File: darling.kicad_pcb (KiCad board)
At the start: 2 copper layers, 24 x 14 mm, 16 parts, among them J1 USB_C_Receptacle_USB2.0, J2 Conn_01x05, U1 FT230XQ

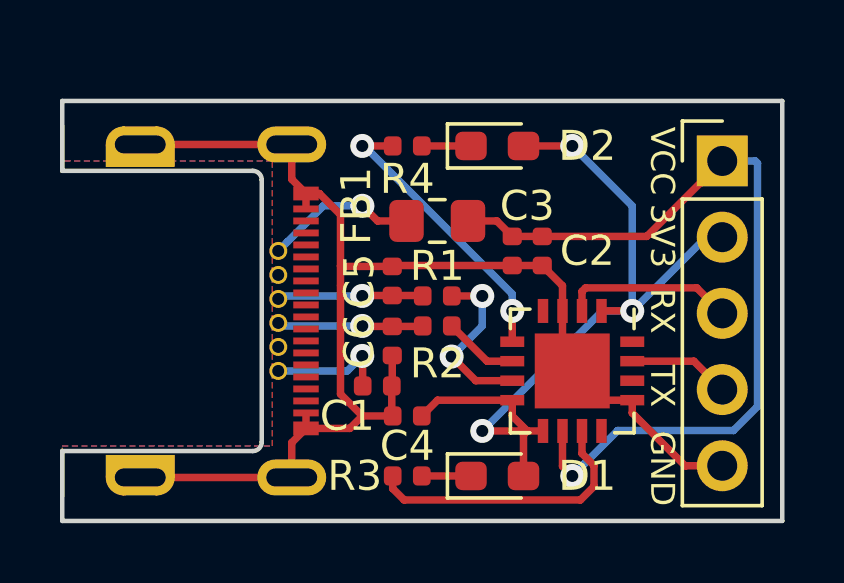
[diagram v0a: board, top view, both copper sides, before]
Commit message: reroute some parts
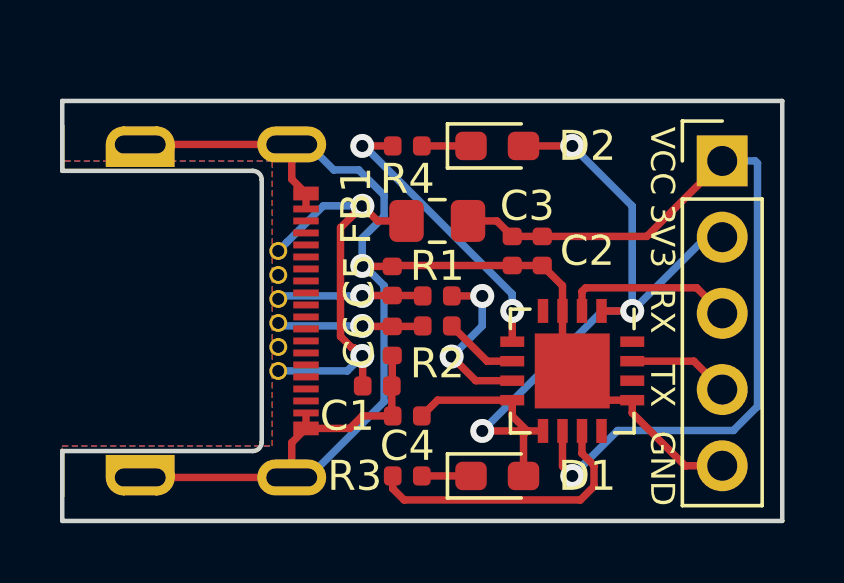
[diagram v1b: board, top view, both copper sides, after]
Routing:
- net GND: track 45.5 -> 51.5 mm, vias 0 -> 1
- net Net-(C1-Pad1): track 9.12 -> 14.8 mm
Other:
- rule trace_min: 0.2 -> 0.125
- rule via_min_size: 0.4 -> 0.6
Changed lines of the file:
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@@
-(kicad_pcb (version 20171130) (host pcbnew 5.1.0)
+(kicad_pcb (version 20171130) (host pcbnew 5.1.1)
   (general
     (thickness 1.6)
     (drawings 23)
-    (tracks 128)
+    (tracks 140)
     (zones 0)
     (modules 16)
@@
     (zone_clearance 0.508)
     (zone_45_only no)
-    (trace_min 0.2)
+    (trace_min 0.125)
     (via_size 0.8)
     (via_drill 0.4)
-    (via_min_size 0.4)
+    (via_min_size 0.6)
     (via_min_drill 0.3)
     (uvia_size 0.3)
@@
   (segment (start 128 125.985) (end 127.985 126) (width 0.25) (layer F.Cu) (net 1))
   (segment (start 128 124.985) (end 128 125.985) (width 0.25) (layer F.Cu) (net 1))
-  (segment (start 126.274999 126.271767) (end 127.003232 127) (width 0.25) (layer F.Cu) (net 1))
-  (segment (start 128 122.015) (end 126.911998 122.015) (width 0.25) (layer F.Cu) (net 1))
-  (segment (start 126.274999 122.651999) (end 126.274999 126.271767) (width 0.25) (layer F.Cu) (net 1))
-  (segment (start 125.57 119.585) (end 126.274999 120.289999) (width 0.25) (layer F.Cu) (net 1))
-  (segment (start 125.125 119.585) (end 125.57 119.585) (width 0.25) (layer F.Cu) (net 1))
-  (segment (start 126.911998 122.015) (end 126.289999 122.015) (width 0.25) (layer F.Cu) (net 1))
-  (segment (start 126.289999 122.015) (end 126.274999 122) (width 0.25) (layer F.Cu) (net 1))
-  (segment (start 126.274999 120.289999) (end 126.274999 122) (width 0.25) (layer F.Cu) (net 1))
-  (segment (start 126.274999 122) (end 126.274999 122.651999) (width 0.25) (layer F.Cu) (net 1))
   (segment (start 125.125 127.415) (end 126.588232 127.415) (width 0.25) (layer F.Cu) (net 1))
   (segment (start 128.03 121.985) (end 128 122.015) (width 0.25) (layer F.Cu) (net 1))
@@
   (segment (start 136 126.9) (end 137.76 128.66) (width 0.25) (layer F.Cu) (net 1))
   (segment (start 136 126.475) (end 136 126.9) (width 0.25) (layer F.Cu) (net 1))
-  (via (at 127.005153 119.994847) (size 0.8) (drill 0.4) (layers F.Cu B.Cu) (net 22))
-  (segment (start 128.475 120.5) (end 127.510306 120.5) (width 0.25) (layer F.Cu) (net 22))
-  (segment (start 127.510306 120.5) (end 127.005153 119.994847) (width 0.25) (layer F.Cu) (net 22))
-  (via (at 127 125) (size 0.8) (drill 0.4) (layers F.Cu B.Cu) (net 22))
-  (segment (start 127.015 126) (end 127.015 125.015) (width 0.25) (layer F.Cu) (net 22))
-  (segment (start 127.015 125.015) (end 127 125) (width 0.25) (layer F.Cu) (net 22))
-  (segment (start 127 125) (end 126.5 125.5) (width 0.25) (layer B.Cu) (net 22))
-  (segment (start 125.705153 119.994847) (end 124.5 121.2) (width 0.25) (layer B.Cu) (net 22))
-  (segment (start 127.005153 119.994847) (end 125.705153 119.994847) (width 0.25) (layer B.Cu) (net 22))
-  (segment (start 124.5 121.2) (end 124.2 121.5) (width 0.25) (layer B.Cu) (net 22))
-  (segment (start 126.5 125.5) (end 124.2 125.5) (width 0.25) (layer B.Cu) (net 22))
+  (segment (start 125.32 119.585) (end 125.125 119.585) (width 0.25) (layer F.Cu) (net 1))
+  (segment (start 125.2 129.05) (end 124.65 129.05) (width 0.25) (layer B.Cu) (net 1))
+  (segment (start 127.725001 126.524999) (end 125.2 129.05) (width 0.25) (layer B.Cu) (net 1))
+  (segment (start 127.725001 122.651999) (end 127.725001 126.524999) (width 0.25) (layer B.Cu) (net 1))
+  (segment (start 127.348001 122.274999) (end 127.725001 122.651999) (width 0.25) (layer B.Cu) (net 1))
+  (via (at 127 122) (size 0.8) (drill 0.4) (layers F.Cu B.Cu) (net 1))
+  (segment (start 128 122.015) (end 127.015 122.015) (width 0.25) (layer F.Cu) (net 1))
+  (segment (start 127.015 122.015) (end 127 122) (width 0.25) (layer F.Cu) (net 1))
+  (segment (start 126.883308 118.8) (end 126.05 118.8) (width 0.25) (layer B.Cu) (net 1))
+  (segment (start 127.730154 119.646846) (end 126.883308 118.8) (width 0.25) (layer B.Cu) (net 1))
+  (segment (start 126.05 118.8) (end 125.2 117.95) (width 0.25) (layer B.Cu) (net 1))
+  (segment (start 127.730154 120.342848) (end 127.730154 119.646846) (width 0.25) (layer B.Cu) (net 1))
+  (segment (start 125.2 117.95) (end 124.65 117.95) (width 0.25) (layer B.Cu) (net 1))
+  (segment (start 127 121.073002) (end 127.730154 120.342848) (width 0.25) (layer B.Cu) (net 1))
+  (segment (start 127 122) (end 127 121.073002) (width 0.25) (layer B.Cu) (net 1))
   (segment (start 133 121.015) (end 132 121.015) (width 0.25) (layer F.Cu) (net 2))
   (segment (start 131.485 120.5) (end 132 121.015) (width 0.25) (layer F.Cu) (net 2))
@@
   (segment (start 132 122.934315) (end 127.065685 118) (width 0.25) (layer B.Cu) (net 17))
   (segment (start 127 118) (end 128.015 118) (width 0.25) (layer F.Cu) (net 17))
+  (via (at 127.005153 119.994847) (size 0.8) (drill 0.4) (layers F.Cu B.Cu) (net 22))
+  (segment (start 128.475 120.5) (end 127.510306 120.5) (width 0.25) (layer F.Cu) (net 22))
+  (segment (start 127.510306 120.5) (end 127.005153 119.994847) (width 0.25) (layer F.Cu) (net 22))
+  (via (at 127 125) (size 0.8) (drill 0.4) (layers F.Cu B.Cu) (net 22))
+  (segment (start 127.015 126) (end 127.015 125.015) (width 0.25) (layer F.Cu) (net 22))
+  (segment (start 127.015 125.015) (end 127 125) (width 0.25) (layer F.Cu) (net 22))
+  (segment (start 127 125) (end 126.5 125.5) (width 0.25) (layer B.Cu) (net 22))
+  (segment (start 125.705153 119.994847) (end 124.5 121.2) (width 0.25) (layer B.Cu) (net 22))
+  (segment (start 127.005153 119.994847) (end 125.705153 119.994847) (width 0.25) (layer B.Cu) (net 22))
+  (segment (start 124.5 121.2) (end 124.2 121.5) (width 0.25) (layer B.Cu) (net 22))
+  (segment (start 126.5 125.5) (end 124.2 125.5) (width 0.25) (layer B.Cu) (net 22))
+  (segment (start 126.605154 120.394846) (end 127.005153 119.994847) (width 0.25) (layer F.Cu) (net 22))
+  (segment (start 126.274999 120.725001) (end 126.605154 120.394846) (width 0.25) (layer F.Cu) (net 22))
+  (segment (start 126.274999 124.348001) (end 126.274999 120.725001) (width 0.25) (layer F.Cu) (net 22))
+  (segment (start 126.651999 124.725001) (end 126.274999 124.348001) (width 0.25) (layer F.Cu) (net 22))
+  (segment (start 126.725001 124.725001) (end 126.651999 124.725001) (width 0.25) (layer F.Cu) (net 22))
+  (segment (start 127 125) (end 126.725001 124.725001) (width 0.25) (layer F.Cu) (net 22))
   (zone (net 1) (net_name GND) (layer F.Cu) (hatch edge 0.508)
     (connect_pads (clearance 0.508))

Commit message: fixed #4 usb-c is now reversable
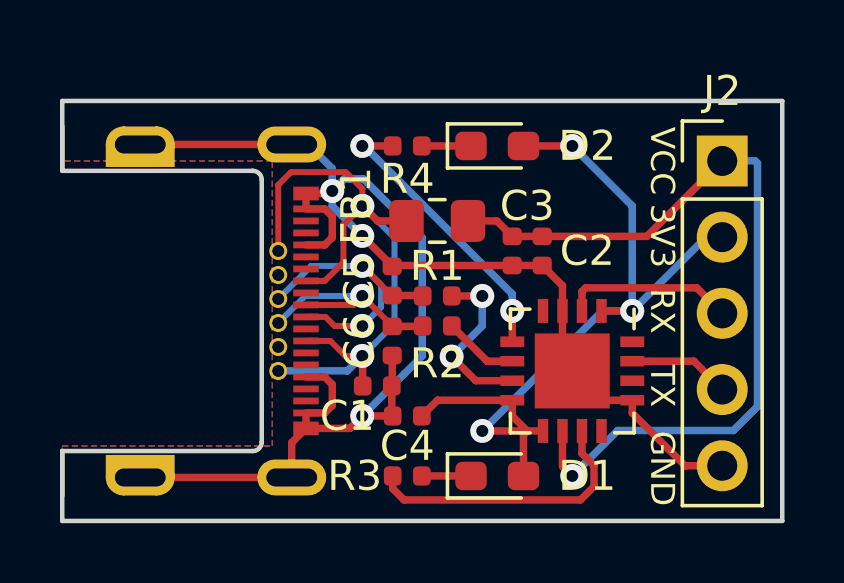
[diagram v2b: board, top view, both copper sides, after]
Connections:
- J2 pad 1: VCC -> (no net)
- J2 pad 2: 3V3 -> (no net)
- J2 pad 3: RX -> (no net)
- J2 pad 4: TX -> (no net)
- J2 pad 5: GND -> (no net)
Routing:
- net Net-(C1-Pad1): track 14.8 -> 23.3 mm
- net Net-(C5-Pad1): track 4.87 -> 10.3 mm, vias 1 -> 2
- net GND: track 51.5 -> 56.5 mm, vias 1 -> 3
- net Net-(C6-Pad1): track 4.87 -> 7.79 mm
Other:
- net class Default: clearance 0.2 -> 0.127; trace_width 0.25 -> 0.2
- net class GND added: clearance 0.2, trace_width 0.25, via_dia 0.8, via_drill 0.4
- rule trace_clearance: 0.2 -> 0.127
